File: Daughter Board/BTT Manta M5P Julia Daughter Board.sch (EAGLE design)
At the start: 41 parts, among them K1 68612014422, X10 JST-XH-03-PIN-LONG-PAD, X11 Z_LIM, X2 EXTRUDER MOTOR, X3 BED THM, X4 24V, X5 24V, X6 24V, X7 24V, X8 JST-XH-03-PIN-LONG-PAD

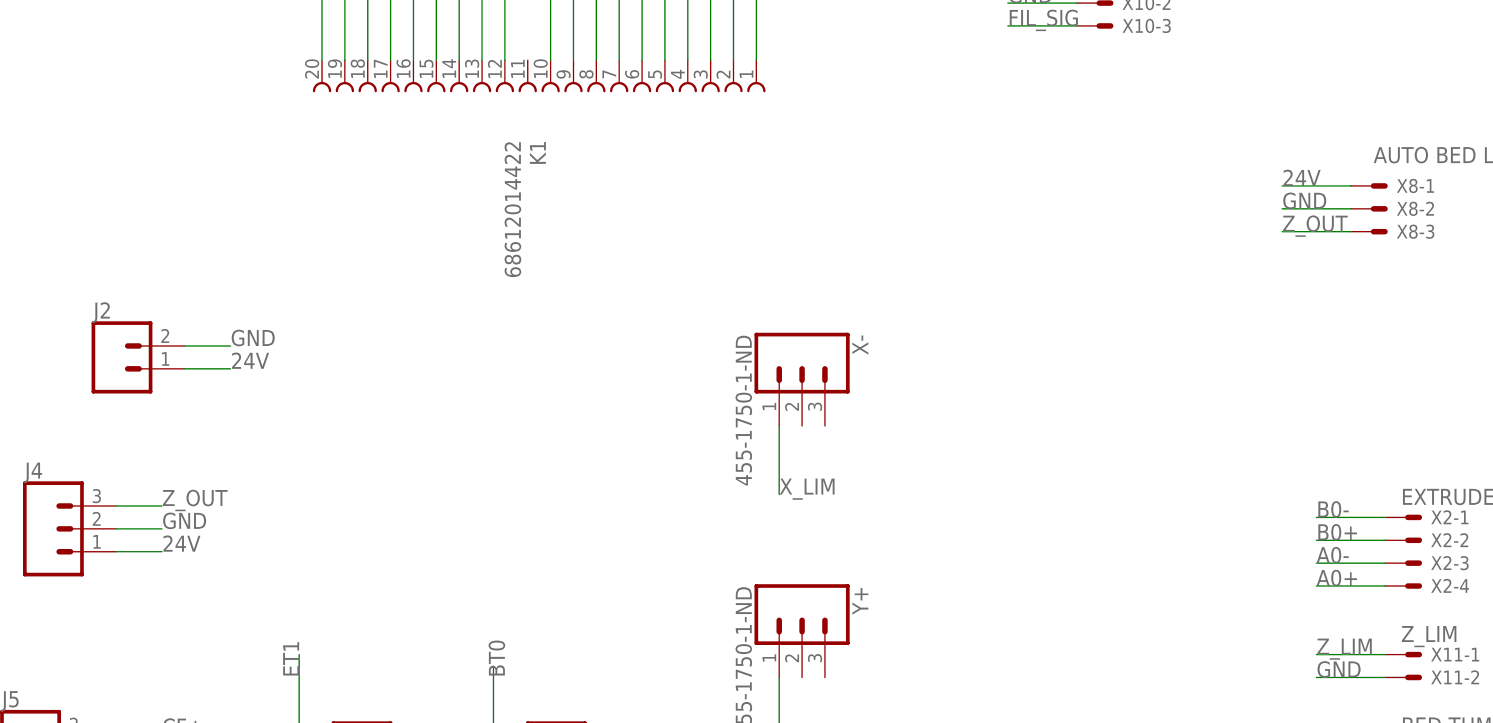
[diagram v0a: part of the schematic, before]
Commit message: Changed Probe pin voltage to 5V
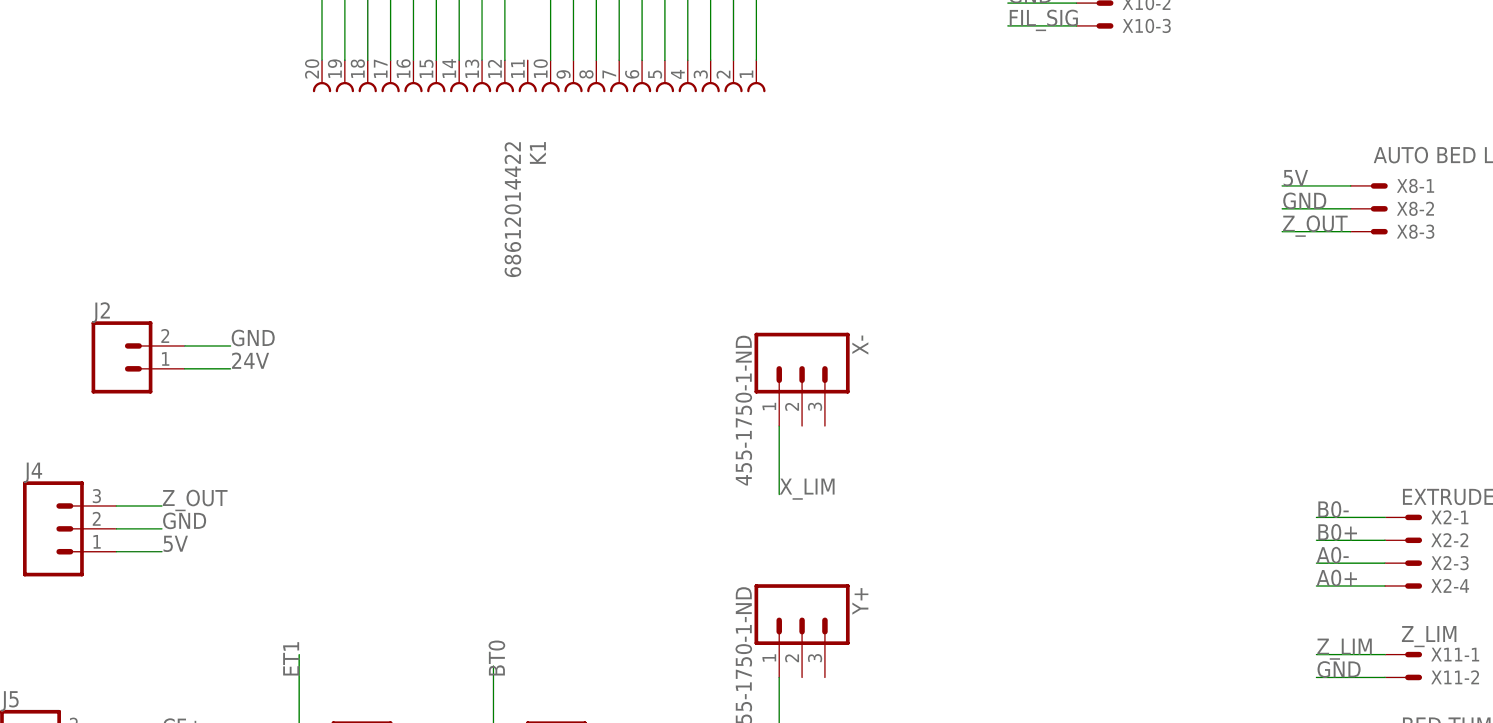
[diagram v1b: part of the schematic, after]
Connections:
- net 24V: no longer J4.1, X8-1.S
- net 5V: now also J4.1, X8-1.S
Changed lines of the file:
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@@
-</segment>
-<segment>
-<pinref part="X8" gate="-1" pin="S"/>
-<wire x1="187.96" y1="320.04" x2="180.34" y2="320.04" width="0.1524" layer="91"/>
-<label x="180.34" y="320.04" size="1.778" layer="95"/>
 </segment>
 <segment>
@@
 <wire x1="58.42" y1="299.72" x2="63.5" y2="299.72" width="0.1524" layer="91"/>
 <label x="63.5" y="299.72" size="1.778" layer="95"/>
-</segment>
-<segment>
-<pinref part="J4" gate="J$1" pin="1"/>
-<wire x1="50.8" y1="279.4" x2="55.88" y2="279.4" width="0.1524" layer="91"/>
-<label x="55.88" y="279.4" size="1.778" layer="95"/>
 </segment>
 </net>
@@
 <label x="149.86" y="342.9" size="1.778" layer="95"/>
 </segment>
-</net>
+<segment>
+<pinref part="X8" gate="-1" pin="S"/>
+<wire x1="187.96" y1="320.04" x2="180.34" y2="320.04" width="0.1524" layer="91"/>
+<label x="180.34" y="320.04" size="1.778" layer="95"/>
+</segment>
+<segment>
+<pinref part="J4" gate="J$1" pin="1"/>
+<wire x1="50.8" y1="279.4" x2="55.88" y2="279.4" width="0.1524" layer="91"/>
+<label x="55.88" y="279.4" size="1.778" layer="95"/>
+</segment>
+</net>
